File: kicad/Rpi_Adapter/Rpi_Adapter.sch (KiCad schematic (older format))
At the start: 12 parts, among them P1 CONN_02X20, P2 CONN_02X03

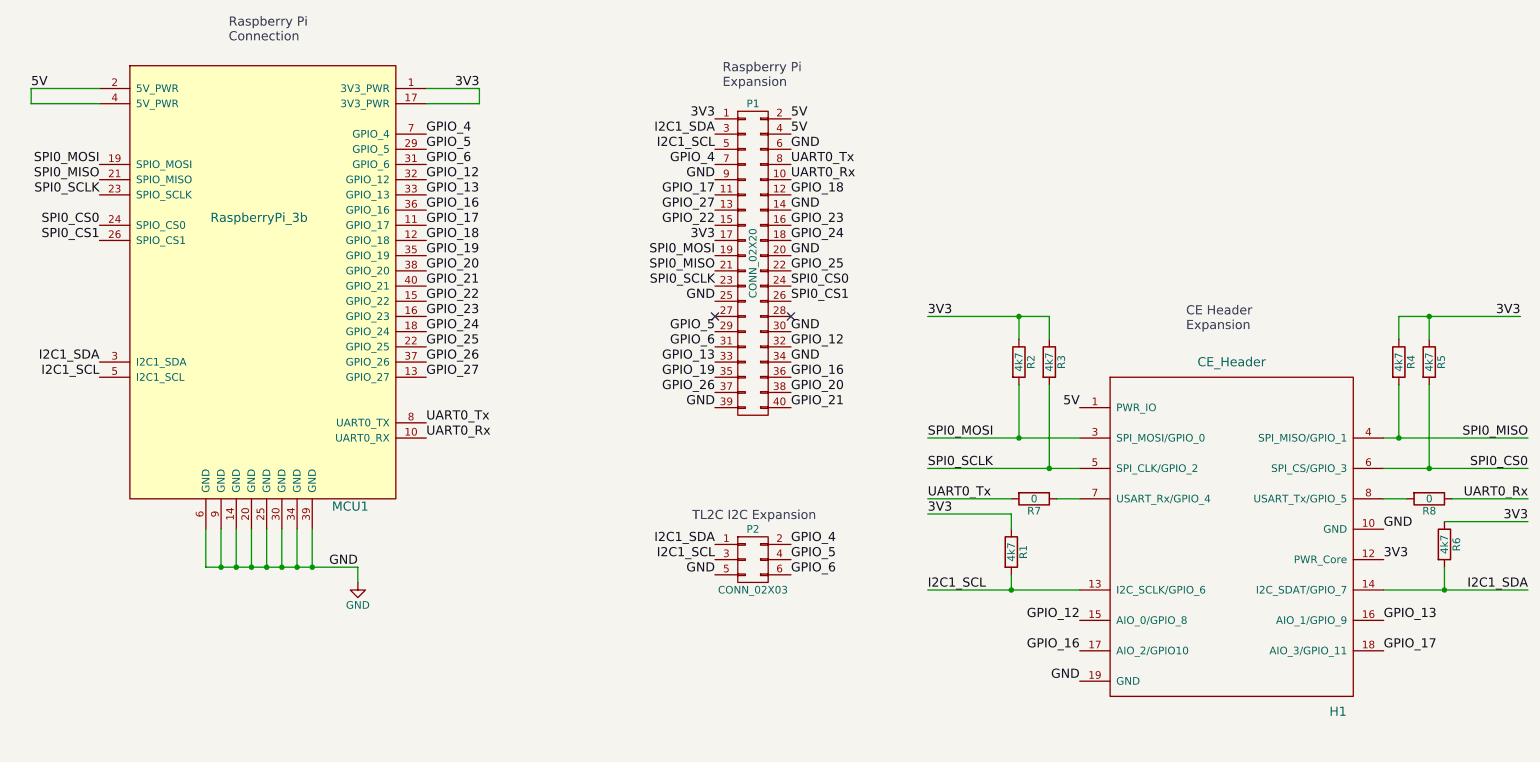
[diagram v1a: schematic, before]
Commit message: Re-worked the RPi Adapter to be more compact.
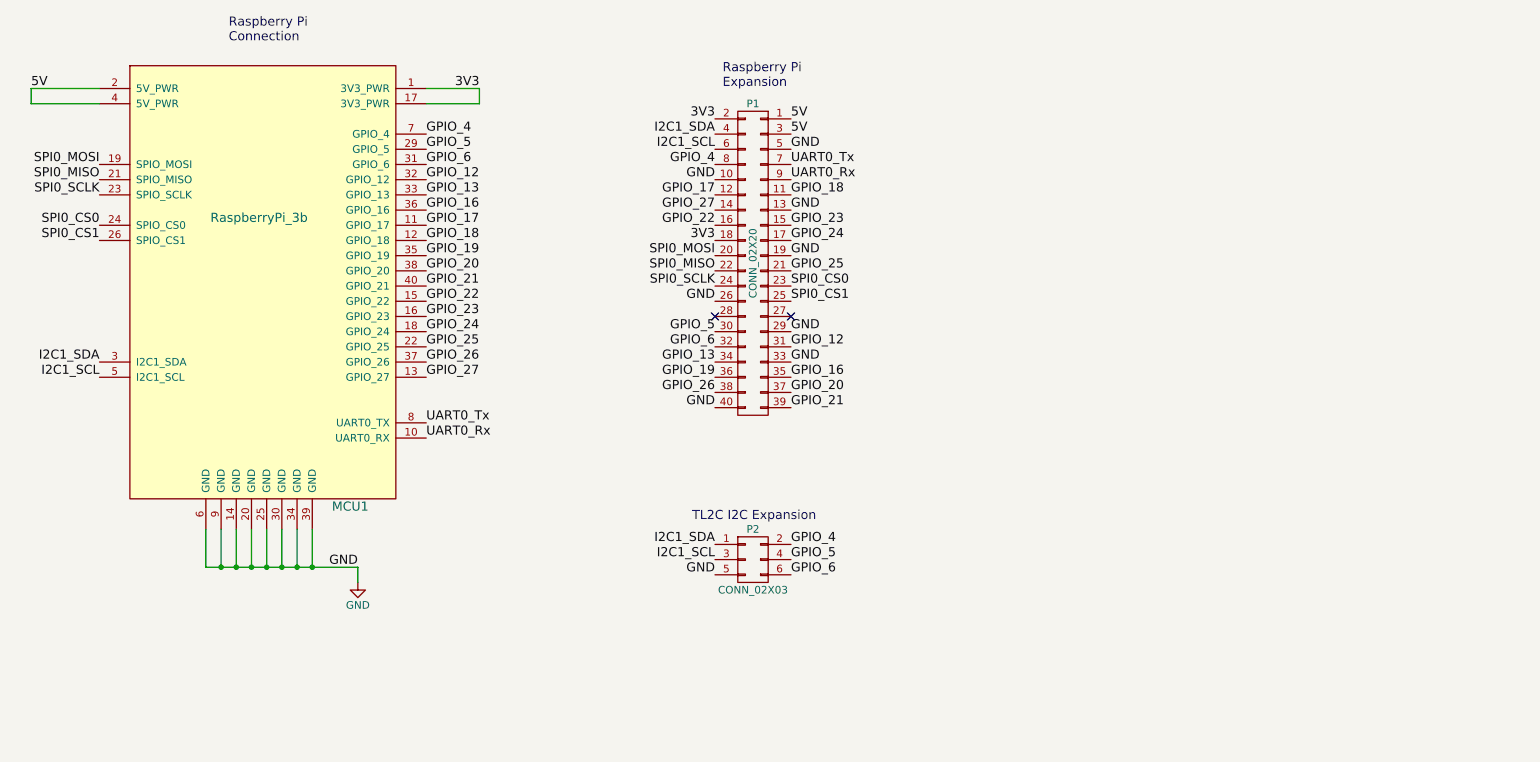
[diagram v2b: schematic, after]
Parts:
- removed H1: CE_Header, CE_Header:CE_Header, symbol CE_Header
- removed R1, R2, R3, R4, R5, R6: 4k7, Resistors_SMD:R_0805, symbol R
- removed R7, R8: 0, Resistors_SMD:R_0805, symbol R
- MCU1: footprint Rpi_Adapter_Footprints:Pin_Header_Straight_2x20_Pitch2.54mm -> Socket_Strips:Socket_Strip_Straight_2x10_Pitch2.54mm_SMD
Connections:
- net 3V3: now also P1.18 (P18), P1.2 (P2); no longer P1.1 (P1), P1.17 (P17)
- net 5V: now also P1.1 (P1), P1.3 (P3); no longer P1.2 (P2), P1.4 (P4)
- net GND: now also P1.10 (P10), P1.13 (P13), P1.19 (P19), P1.26 (P26), P1.29 (P29), P1.33 (P33), P1.40 (P40), P1.5 (P5); no longer P1.14 (P14), P1.20 (P20), P1.25 (P25), P1.30 (P30), P1.34 (P34), P1.39 (P39), P1.6 (P6), P1.9 (P9)
- net GPIO_12: now also P1.31 (P31); no longer P1.32 (P32)
- net GPIO_13: now also P1.34 (P34); no longer P1.33 (P33)
- net GPIO_16: now also P1.35 (P35); no longer P1.36 (P36)
- net GPIO_17: now also P1.12 (P12); no longer P1.11 (P11)
- net GPIO_18: now also P1.11 (P11); no longer P1.12 (P12)
- net GPIO_19: now also P1.36 (P36); no longer P1.35 (P35)
- net GPIO_20: now also P1.37 (P37); no longer P1.38 (P38)
- net GPIO_21: now also P1.39 (P39); no longer P1.40 (P40)
- net GPIO_22: now also P1.16 (P16); no longer P1.15 (P15)
- net GPIO_23: now also P1.15 (P15); no longer P1.16 (P16)
- net GPIO_24: now also P1.17 (P17); no longer P1.18 (P18)
- net GPIO_25: now also P1.21 (P21); no longer P1.22 (P22)
- net GPIO_26: now also P1.38 (P38); no longer P1.37 (P37)
- net GPIO_27: now also P1.14 (P14); no longer P1.13 (P13)
- net GPIO_4: now also P1.8 (P8); no longer P1.7 (P7)
- net GPIO_5: now also P1.30 (P30); no longer P1.29 (P29)
- net GPIO_6: now also P1.32 (P32); no longer P1.31 (P31)
- net I2C1_SCL: now also P1.6 (P6); no longer P1.5 (P5)
- net I2C1_SDA: now also P1.4 (P4); no longer P1.3 (P3)
- net SPI0_CS0: now also P1.23 (P23); no longer P1.24 (P24)
- net SPI0_CS1: now also P1.25 (P25); no longer P1.26 (P26)
- net SPI0_MISO: now also P1.22 (P22); no longer P1.21 (P21)
- net SPI0_MOSI: now also P1.20 (P20); no longer P1.19 (P19)
- net SPI0_SCLK: now also P1.24 (P24); no longer P1.23 (P23)
- net UART0_Rx: now also P1.9 (P9); no longer P1.10 (P10)
- net UART0_Tx: now also P1.7 (P7); no longer P1.8 (P8)
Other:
- note removed: "CE Header\nExpansion"
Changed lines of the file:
@@
 F 0 "MCU1" H 3200 1350 60  0000 C CNN
 F 1 "RaspberryPi_3b" H 2600 3250 60  0000 C CNN
-F 2 "Rpi_Adapter_Footprints:Pin_Header_Straight_2x20_Pitch2.54mm" H 2250 3800 60  0001 C CNN
+F 2 "Socket_Strips:Socket_Strip_Straight_2x10_Pitch2.54mm_SMD" H 2250 3800 60  0001 C CNN
 F 3 "" H 2250 3800 60  0000 C CNN
 	1    2650 2800
-	1    0    0    -1
-$EndComp
-$Comp
-L CE_Header H1
-U 1 1 594798FD
-P 9000 4400
-F 0 "H1" H 9700 3200 60  0000 C CNN
-F 1 "CE_Header" H 9000 5500 60  0000 C CNN
-F 2 "CE_Header:CE_Header" H 8600 4800 60  0001 C CNN
-F 3 "" H 8600 4800 60  0000 C CNN
-	1    9000 4400
 	1    0    0    -1
 $EndComp
@@
 F 3 "" H 5850 1700 60  0000 C CNN
 	1    5850 2650
-	1    0    0    -1
+	-1   0    0    -1
 $EndComp
 Text Label 5600 1700 2    60   ~ 0
@@
 I2C1_SCL
 $Comp
-L GND #PWR1
+L GND #PWR01
 U 1 1 5947A28B
 P 3250 4750
-F 0 "#PWR1" H 3250 4500 50  0001 C CNN
+F 0 "#PWR01" H 3250 4500 50  0001 C CNN
 F 1 "GND" H 3250 4600 50  0000 C CNN
 F 2 "" H 3250 4750 60  0000 C CNN
@@
 Text Label 3700 2800 0    60   ~ 0
 GPIO_21
-Text Label 8000 3600 2    60   ~ 0
-5V
-Text Label 10000 4600 0    60   ~ 0
-3V3
-Text Label 7000 3800 0    60   ~ 0
-SPI0_MOSI
-Text Label 10950 3800 2    60   ~ 0
-SPI0_MISO
-Text Label 7000 4000 0    60   ~ 0
-SPI0_SCLK
-Text Label 7000 4200 0    60   ~ 0
-UART0_Tx
-Text Label 10950 4200 2    60   ~ 0
-UART0_Rx
-Text Label 8000 5400 2    60   ~ 0
-GND
-Text Label 10000 4400 0    60   ~ 0
-GND
-Text Label 10950 4800 2    60   ~ 0
-I2C1_SDA
-Text Label 7000 4800 0    60   ~ 0
-I2C1_SCL
-Text Label 10950 4000 2    60   ~ 0
-SPI0_CS0
 Text Label 5600 4500 2    60   ~ 0
 I2C1_SDA
@@
 Text Label 6100 4700 0    60   ~ 0
 GPIO_6
-Text Label 8000 5000 2    60   ~ 0
-GPIO_12
-Text Label 10000 5000 0    60   ~ 0
-GPIO_13
-Text Label 8000 5200 2    60   ~ 0
-GPIO_16
-Text Label 10000 5200 0    60   ~ 0
-GPIO_17
 Text Notes 5650 1500 0    60   ~ 0
 Raspberry Pi\nExpansion
 Text Notes 5450 4350 0    60   ~ 0
 TL2C I2C Expansion
-Text Notes 8700 3100 0    60   ~ 0
-CE Header\nExpansion
 Text Notes 2400 1200 0    60   ~ 0
 Raspberry Pi\nConnection
@@
 Wire Wire Line
 	4050 1500 3700 1500
-Wire Wire Line
-	8000 3800 7000 3800
-Wire Wire Line
-	8000 4000 7000 4000
-Wire Wire Line
-	10000 3800 10950 3800
-Wire Wire Line
-	10000 4000 10950 4000
-Wire Wire Line
-	10000 4800 10950 4800
-Wire Wire Line
-	8000 4800 7000 4800
-$Comp
-L R R2
-U 1 1 594806C0
-P 7600 3300
-F 0 "R2" V 7680 3300 50  0000 C CNN
-F 1 "4k7" V 7600 3300 50  0000 C CNN
-F 2 "Resistors_SMD:R_0805" V 7530 3300 30  0001 C CNN
-F 3 "" H 7600 3300 30  0000 C CNN
-	1    7600 3300
-	1    0    0    -1
-$EndComp
-$Comp
-L R R3
-U 1 1 59480738
-P 7800 3300
-F 0 "R3" V 7880 3300 50  0000 C CNN
-F 1 "4k7" V 7800 3300 50  0000 C CNN
-F 2 "Resistors_SMD:R_0805" V 7730 3300 30  0001 C CNN
-F 3 "" H 7800 3300 30  0000 C CNN
-	1    7800 3300
-	1    0    0    -1
-$EndComp
-Wire Wire Line
-	7600 3450 7600 3800
-Connection ~ 7600 3800
-Wire Wire Line
-	7800 3450 7800 4000
-Connection ~ 7800 4000
-Wire Wire Line
-	7800 3000 7800 3150
-Wire Wire Line
-	7000 3000 7800 3000
-Wire Wire Line
-	7600 3000 7600 3150
-Connection ~ 7600 3000
-Text Label 7000 3000 0    60   ~ 0
-3V3
-$Comp
-L R R1
-U 1 1 594808E4
-P 7550 4550
-F 0 "R1" V 7630 4550 50  0000 C CNN
-F 1 "4k7" V 7550 4550 50  0000 C CNN
-F 2 "Resistors_SMD:R_0805" V 7480 4550 30  0001 C CNN
-F 3 "" H 7550 4550 30  0000 C CNN
-	1    7550 4550
-	1    0    0    -1
-$EndComp
-Wire Wire Line
-	7550 4800 7550 4700
-Connection ~ 7550 4800
-Wire Wire Line
-	7550 4400 7550 4300
-Wire Wire Line
-	7550 4300 7000 4300
-Text Label 7000 4300 0    60   ~ 0
-3V3
-$Comp
-L R R4
-U 1 1 594809B3
-P 10100 3300
-F 0 "R4" V 10180 3300 50  0000 C CNN
-F 1 "4k7" V 10100 3300 50  0000 C CNN
-F 2 "Resistors_SMD:R_0805" V 10030 3300 30  0001 C CNN
-F 3 "" H 10100 3300 30  0000 C CNN
-	1    10100 3300
-	1    0    0    -1
-$EndComp
-$Comp
-L R R5
-U 1 1 59480A2F
-P 10300 3300
-F 0 "R5" V 10380 3300 50  0000 C CNN
-F 1 "4k7" V 10300 3300 50  0000 C CNN
-F 2 "Resistors_SMD:R_0805" V 10230 3300 30  0001 C CNN
-F 3 "" H 10300 3300 30  0000 C CNN
-	1    10300 3300
-	1    0    0    -1
-$EndComp
-Wire Wire Line
-	10100 3450 10100 3800
-Connection ~ 10100 3800
-Wire Wire Line
-	10300 3450 10300 4000
-Connection ~ 10300 4000
-Wire Wire Line
-	10100 3150 10100 3000
-Wire Wire Line
-	10100 3000 10900 3000
-Wire Wire Line
-	10300 3000 10300 3150
-Connection ~ 10300 3000
-$Comp
-L R R6
-U 1 1 59480C1D
-P 10400 4500
-F 0 "R6" V 10480 4500 50  0000 C CNN
-F 1 "4k7" V 10400 4500 50  0000 C CNN
-F 2 "Resistors_SMD:R_0805" V 10330 4500 30  0001 C CNN
-F 3 "" H 10400 4500 30  0000 C CNN
-	1    10400 4500
-	1    0    0    -1
-$EndComp
-Wire Wire Line
-	10400 4800 10400 4650
-Connection ~ 10400 4800
-Wire Wire Line
-	10400 4350 10950 4350
-Text Label 10950 4350 2    60   ~ 0
-3V3
-Text Label 10900 3000 2    60   ~ 0
-3V3
-$Comp
-L R R8
-U 1 1 59483847
-P 10300 4200
-F 0 "R8" V 10380 4200 50  0000 C CNN
-F 1 "0" V 10300 4200 50  0000 C CNN
-F 2 "Resistors_SMD:R_0805" V 10230 4200 30  0001 C CNN
-F 3 "" H 10300 4200 30  0000 C CNN
-	1    10300 4200
-	0    1    1    0
-$EndComp
-Wire Wire Line
-	10000 4200 10150 4200
-Wire Wire Line
-	10450 4200 10950 4200
-$Comp
-L R R7
-U 1 1 59483A0A
-P 7700 4200
-F 0 "R7" V 7780 4200 50  0000 C CNN
-F 1 "0" V 7700 4200 50  0000 C CNN
-F 2 "Resistors_SMD:R_0805" V 7630 4200 30  0001 C CNN
-F 3 "" H 7700 4200 30  0000 C CNN
-	1    7700 4200
-	0    1    1    0
-$EndComp
-Wire Wire Line
-	8000 4200 7850 4200
-Wire Wire Line
-	7550 4200 7000 4200
 $EndSCHEMATC

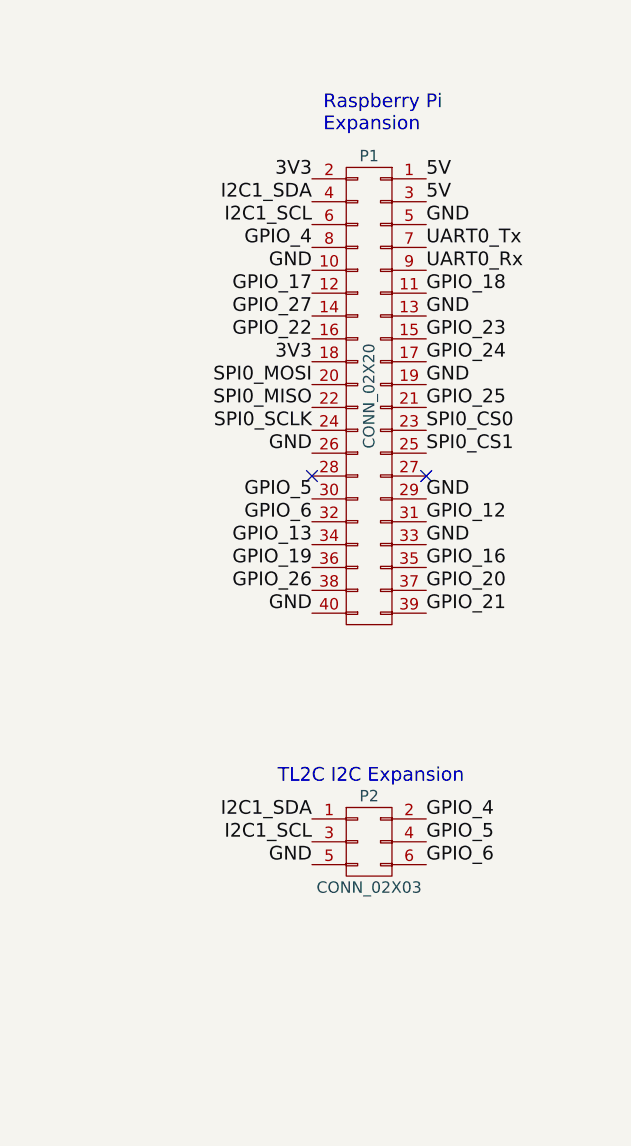
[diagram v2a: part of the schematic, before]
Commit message: Reworked the RPi Adapter 2L_4 for RJ45
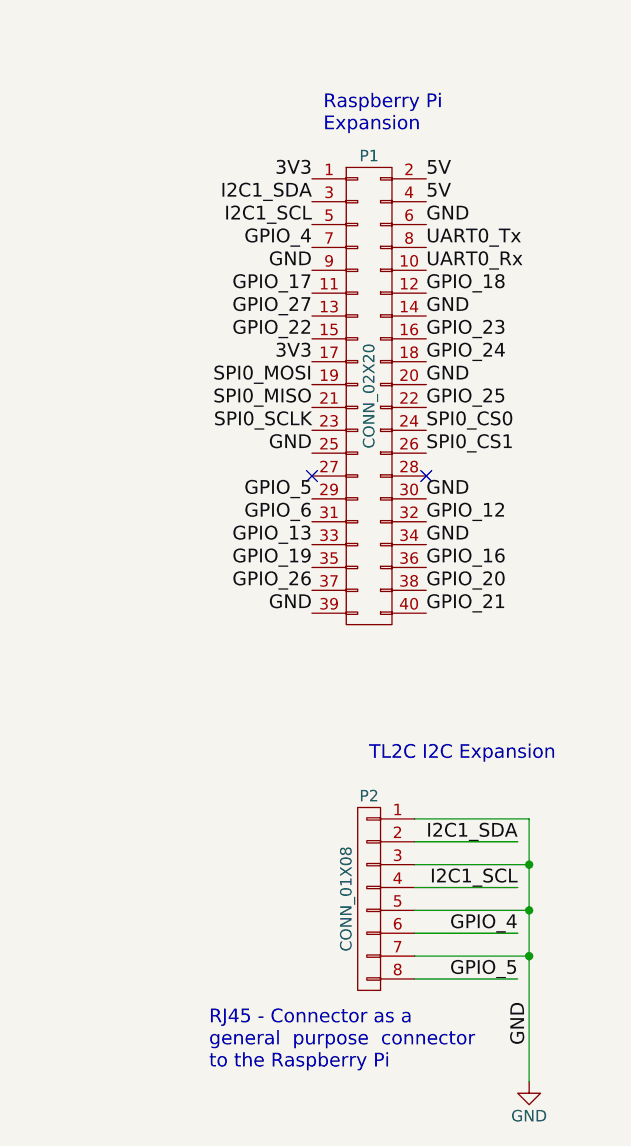
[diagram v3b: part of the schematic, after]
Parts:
- removed P2: CONN_02X03, Pin_Headers:Pin_Header_Straight_2x03_Pitch2.54mm, symbol CONN_02X03
- added P2: CONN_01X08, tl2c-footprint:RJ45_8P8C, symbol CONN_01X08
- MCU1: footprint Socket_Strips:Socket_Strip_Straight_2x10_Pitch2.54mm_SMD -> Socket_Strips:Socket_Strip_Straight_2x20_Pitch2.54mm
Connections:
- net 3V3: now also P1.1 (P1), P1.17 (P17); no longer P1.18 (P18), P1.2 (P2)
- net 5V: now also P1.2 (P2), P1.4 (P4); no longer P1.1 (P1), P1.3 (P3)
- net GND: now also P1.14 (P14), P1.20 (P20), P1.25 (P25), P1.30 (P30), P1.34 (P34), P1.39 (P39), P1.6 (P6), P1.9 (P9), P2.1 (P1), P2.3 (P3), P2.5 (P5), P2.7 (P7); no longer P1.10 (P10), P1.13 (P13), P1.19 (P19), P1.26 (P26), P1.29 (P29), P1.33 (P33), P1.40 (P40), P1.5 (P5)
- net GPIO_12: now also P1.32 (P32); no longer P1.31 (P31)
- net GPIO_13: now also P1.33 (P33); no longer P1.34 (P34)
- net GPIO_16: now also P1.36 (P36); no longer P1.35 (P35)
- net GPIO_17: now also P1.11 (P11); no longer P1.12 (P12)
- net GPIO_18: now also P1.12 (P12); no longer P1.11 (P11)
- net GPIO_19: now also P1.35 (P35); no longer P1.36 (P36)
- net GPIO_20: now also P1.38 (P38); no longer P1.37 (P37)
- net GPIO_21: now also P1.40 (P40); no longer P1.39 (P39)
- net GPIO_22: now also P1.15 (P15); no longer P1.16 (P16)
- net GPIO_23: now also P1.16 (P16); no longer P1.15 (P15)
- net GPIO_24: now also P1.18 (P18); no longer P1.17 (P17)
- net GPIO_25: now also P1.22 (P22); no longer P1.21 (P21)
- net GPIO_26: now also P1.37 (P37); no longer P1.38 (P38)
- net GPIO_27: now also P1.13 (P13); no longer P1.14 (P14)
- net GPIO_4: now also P1.7 (P7), P2.6 (P6); no longer P1.8 (P8)
- net GPIO_5: now also P1.29 (P29), P2.8 (P8); no longer P1.30 (P30)
- net GPIO_6: now also P1.31 (P31); no longer P1.32 (P32)
- net I2C1_SCL: now also P1.5 (P5), P2.4 (P4); no longer P1.6 (P6)
- net I2C1_SDA: now also P1.3 (P3), P2.2 (P2); no longer P1.4 (P4)
- net SPI0_CS0: now also P1.24 (P24); no longer P1.23 (P23)
- net SPI0_CS1: now also P1.26 (P26); no longer P1.25 (P25)
- net SPI0_MISO: now also P1.21 (P21); no longer P1.22 (P22)
- net SPI0_MOSI: now also P1.19 (P19); no longer P1.20 (P20)
- net SPI0_SCLK: now also P1.23 (P23); no longer P1.24 (P24)
- net UART0_Rx: now also P1.10 (P10); no longer P1.9 (P9)
- net UART0_Tx: now also P1.8 (P8); no longer P1.7 (P7)
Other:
- note added: "RJ45 - Connector as a \ngeneral purpose connector \nto the Raspberry Pi"
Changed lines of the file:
@@
 F 0 "MCU1" H 3200 1350 60  0000 C CNN
 F 1 "RaspberryPi_3b" H 2600 3250 60  0000 C CNN
-F 2 "Socket_Strips:Socket_Strip_Straight_2x10_Pitch2.54mm_SMD" H 2250 3800 60  0001 C CNN
+F 2 "Socket_Strips:Socket_Strip_Straight_2x20_Pitch2.54mm" H 2250 3800 60  0001 C CNN
 F 3 "" H 2250 3800 60  0000 C CNN
 	1    2650 2800
-	1    0    0    -1
-$EndComp
-$Comp
-L CONN_02X03 P2
-U 1 1 594799AC
-P 5850 4600
-F 0 "P2" H 5850 4800 50  0000 C CNN
-F 1 "CONN_02X03" H 5850 4400 50  0000 C CNN
-F 2 "Pin_Headers:Pin_Header_Straight_2x03_Pitch2.54mm" H 5850 3400 60  0001 C CNN
-F 3 "" H 5850 3400 60  0000 C CNN
-	1    5850 4600
 	1    0    0    -1
 $EndComp
@@
 F 3 "" H 5850 1700 60  0000 C CNN
 	1    5850 2650
-	-1   0    0    -1
+	1    0    0    -1
 $EndComp
 Text Label 5600 1700 2    60   ~ 0
@@
 Text Label 3700 2800 0    60   ~ 0
 GPIO_21
-Text Label 5600 4500 2    60   ~ 0
+Text Label 6500 4600 2    60   ~ 0
 I2C1_SDA
-Text Label 5600 4600 2    60   ~ 0
-I2C1_SCL
-Text Label 5600 4700 2    60   ~ 0
-GND
-Text Label 6100 4500 0    60   ~ 0
+Text Label 6550 5300 3    60   ~ 0
+GND
+Text Label 6500 5000 2    60   ~ 0
 GPIO_4
-Text Label 6100 4600 0    60   ~ 0
+Text Label 6500 5200 2    60   ~ 0
 GPIO_5
-Text Label 6100 4700 0    60   ~ 0
-GPIO_6
 Text Notes 5650 1500 0    60   ~ 0
 Raspberry Pi\nExpansion
-Text Notes 5450 4350 0    60   ~ 0
+Text Notes 5850 4250 0    60   ~ 0
 TL2C I2C Expansion
 Text Notes 2400 1200 0    60   ~ 0
@@
 Wire Wire Line
 	4050 1500 3700 1500
+Text Notes 5150 5600 0    60   ~ 0
+RJ45 - Connector as a \ngeneral  purpose  connector \nto the Raspberry Pi
+$Comp
+L GND #PWR02
+U 1 1 5997F2C0
+P 6550 5650
+F 0 "#PWR02" H 6550 5400 50  0001 C CNN
+F 1 "GND" H 6550 5500 50  0000 C CNN
+F 2 "" H 6550 5650 60  0000 C CNN
+F 3 "" H 6550 5650 60  0000 C CNN
+	1    6550 5650
+	1    0    0    -1
+$EndComp
+$Comp
+L CONN_01X08 P2
+U 1 1 5997F300
+P 5850 4850
+F 0 "P2" H 5850 5300 50  0000 C CNN
+F 1 "CONN_01X08" V 5950 4850 50  0000 C CNN
+F 2 "tl2c-footprint:RJ45_8P8C" H 5850 4850 60  0001 C CNN
+F 3 "" H 5850 4850 60  0000 C CNN
+	1    5850 4850
+	-1   0    0    -1
+$EndComp
+Wire Wire Line
+	6050 4500 6550 4500
+Wire Wire Line
+	6550 4500 6550 5650
+Wire Wire Line
+	6050 4700 6550 4700
+Connection ~ 6550 4700
+Wire Wire Line
+	6050 4900 6550 4900
+Connection ~ 6550 4900
+Wire Wire Line
+	6050 5100 6550 5100
+Connection ~ 6550 5100
+Wire Wire Line
+	6050 4600 6500 4600
+Wire Wire Line
+	6050 4800 6500 4800
+Wire Wire Line
+	6050 5000 6500 5000
+Wire Wire Line
+	6050 5200 6500 5200
+Text Label 6500 4800 2    60   ~ 0
+I2C1_SCL
 $EndSCHEMATC
